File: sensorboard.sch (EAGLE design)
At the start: 34 parts, among them U1 LM1117MP-3.3, U2 LM324D

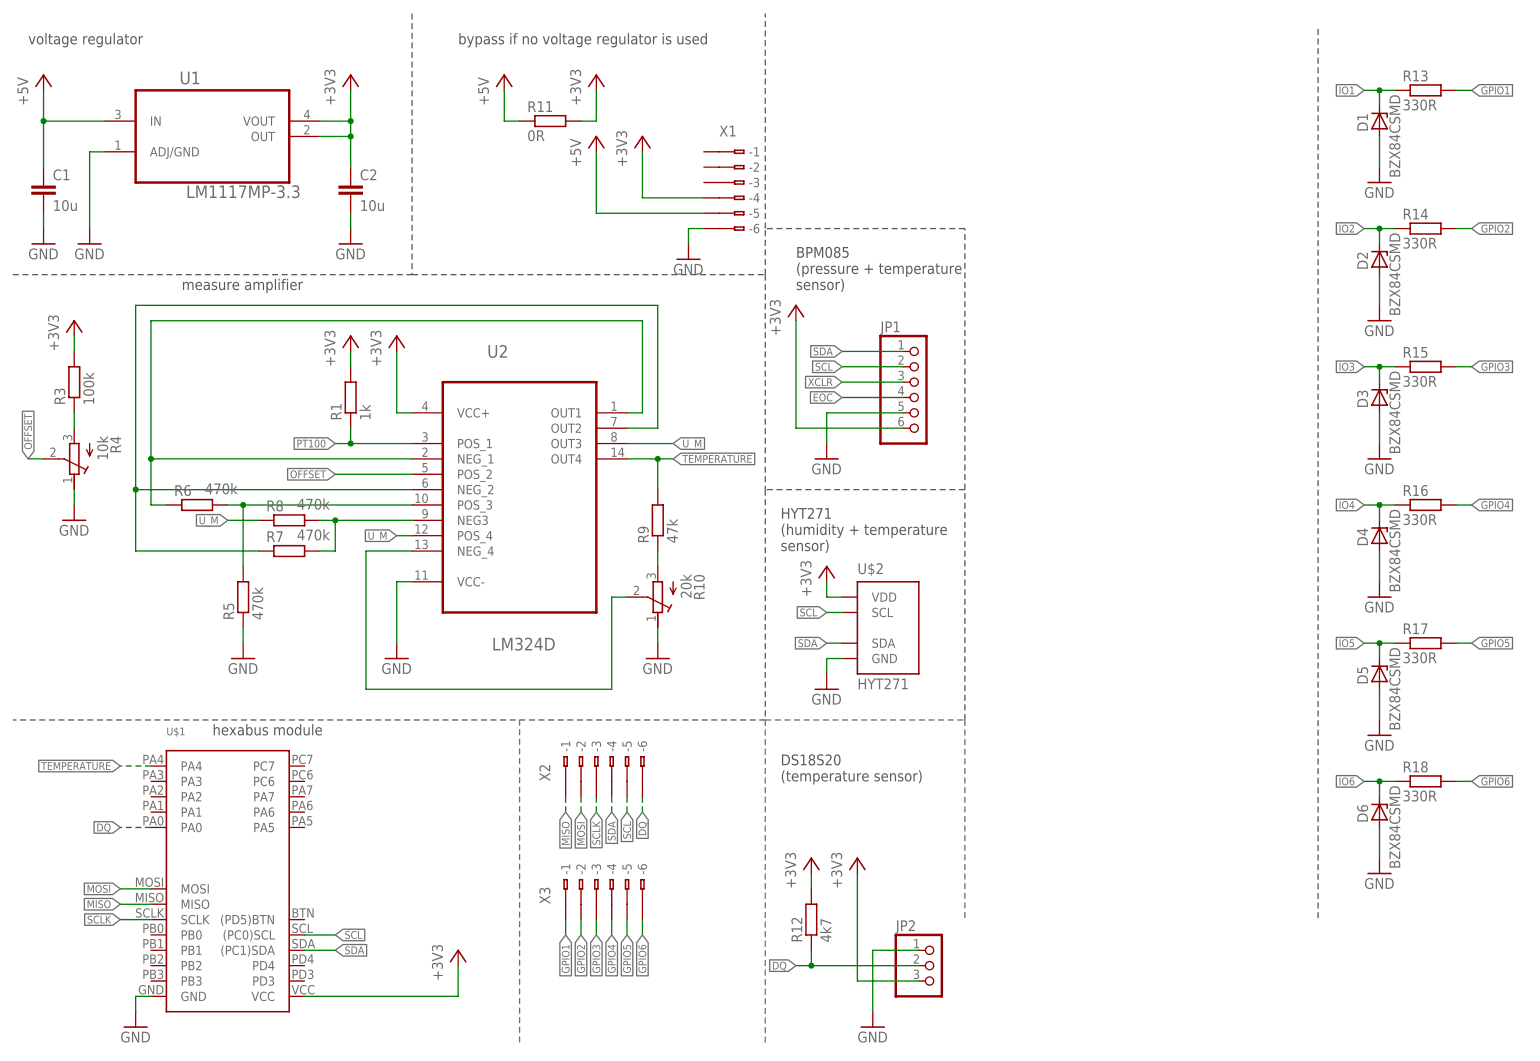
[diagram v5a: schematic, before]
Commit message: added button
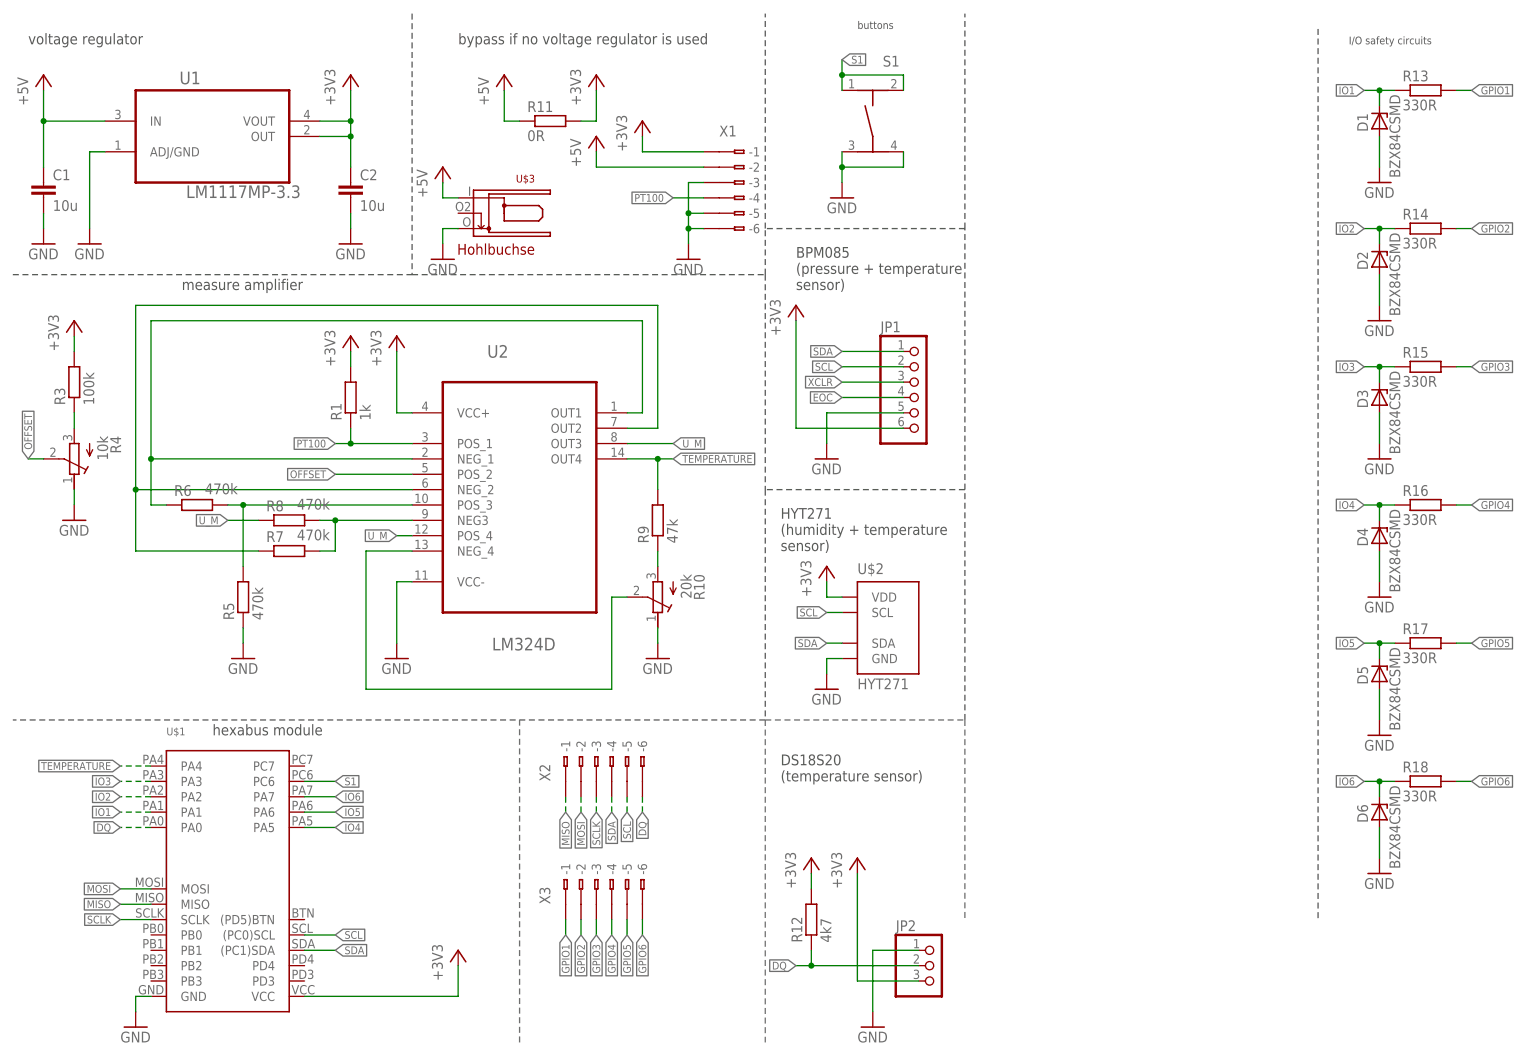
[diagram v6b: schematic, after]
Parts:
- added S1: (no value), Ergaenzung:TASTER-9314_SMD
- added U$3: HOHLBUCHSE, Ergaenzung:HOHLBUCHSE
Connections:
- new net S1: S1.1, S1.2, U$1.PC6
- net +3V3: now also X1.B-1; no longer X1.B-4
- net +5V: now also U$3.I, X1.B-2; no longer X1.B-5
- net GND: now also S1.3, S1.4, U$3.O, X1.B-3, X1.B-5
- net IO1: now also U$1.PA1
- net IO2: now also U$1.PA2
- net IO3: now also U$1.PA3
- net IO4: now also U$1.PA5
- net IO5: now also U$1.PA6
- net IO6: now also U$1.PA7
- net PT100: now also X1.B-4
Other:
- note added: "I/O safety circuits"
- note added: "buttons"
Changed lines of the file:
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@@
 <part name="R16" library="rcl" deviceset="R-EU_" device="R0805" value="330R"/>
 <part name="GND18" library="supply1" deviceset="GND" device=""/>
+<part name="S1" library="Ergaenzung" deviceset="TASTER-9314_SMD" device=""/>
+<part name="U$3" library="Ergaenzung" deviceset="HOHLBUCHSE" device=""/>
+<part name="P+4" library="supply1" deviceset="+5V" device=""/>
+<part name="GND19" library="supply1" deviceset="GND" device=""/>
+<part name="GND20" library="supply1" deviceset="GND" device=""/>
 </parts>
 <sheets>
@@
 <wire x1="162.56" y1="139.7" x2="129.54" y2="139.7" width="0.1524" layer="97" style="longdash"/>
 <wire x1="220.98" y1="172.72" x2="220.98" y2="25.4" width="0.1524" layer="97" style="longdash"/>
+<wire x1="162.56" y1="139.7" x2="162.56" y2="175.26" width="0.1524" layer="97" style="longdash"/>
+<text x="226.06" y="170.18" size="1.27" layer="97">I/O safety circuits</text>
+<text x="144.78" y="172.72" size="1.27" layer="97">buttons</text>
 </plain>
 <instances>
@@
 <instance part="X1" gate="G$1" x="127" y="147.32"/>
 <instance part="GND10" gate="1" x="116.84" y="134.62"/>
-<instance part="+3V10" gate="G$1" x="109.22" y="154.94"/>
+<instance part="+3V10" gate="G$1" x="109.22" y="157.48"/>
 <instance part="P+3" gate="1" x="101.6" y="154.94"/>
 <instance part="U$2" gate="A" x="149.86" y="73.66"/>
@@
 <instance part="R16" gate="G$1" x="238.76" y="93.98"/>
 <instance part="GND18" gate="1" x="231.14" y="78.74"/>
+<instance part="S1" gate="G$1" x="147.32" y="157.48"/>
+<instance part="U$3" gate="G$1" x="91.44" y="142.24" rot="R180"/>
+<instance part="P+4" gate="1" x="76.2" y="149.86"/>
+<instance part="GND19" gate="1" x="76.2" y="134.62"/>
+<instance part="GND20" gate="1" x="142.24" y="144.78"/>
 </instances>
 <busses>
@@
 <wire x1="119.38" y1="139.7" x2="116.84" y2="139.7" width="0.1524" layer="91"/>
 <wire x1="116.84" y1="139.7" x2="116.84" y2="137.16" width="0.1524" layer="91"/>
+<pinref part="X1" gate="G$1" pin="B-3"/>
+<wire x1="119.38" y1="147.32" x2="116.84" y2="147.32" width="0.1524" layer="91"/>
+<wire x1="116.84" y1="147.32" x2="116.84" y2="142.24" width="0.1524" layer="91"/>
+<junction x="116.84" y="139.7"/>
+<pinref part="X1" gate="G$1" pin="B-5"/>
+<wire x1="116.84" y1="142.24" x2="116.84" y2="139.7" width="0.1524" layer="91"/>
+<wire x1="119.38" y1="142.24" x2="116.84" y2="142.24" width="0.1524" layer="91"/>
+<junction x="116.84" y="142.24"/>
 </segment>
 <segment>
@@
 <pinref part="GND18" gate="1" pin="GND"/>
 <wire x1="231.14" y1="86.36" x2="231.14" y2="81.28" width="0.1524" layer="91"/>
+</segment>
+<segment>
+<pinref part="U$3" gate="G$1" pin="O"/>
+<pinref part="GND19" gate="1" pin="GND"/>
+<wire x1="78.74" y1="139.7" x2="76.2" y2="139.7" width="0.1524" layer="91"/>
+<wire x1="76.2" y1="139.7" x2="76.2" y2="137.16" width="0.1524" layer="91"/>
+</segment>
+<segment>
+<pinref part="S1" gate="G$1" pin="4"/>
+<wire x1="152.4" y1="152.4" x2="152.4" y2="149.86" width="0.1524" layer="91"/>
+<wire x1="152.4" y1="149.86" x2="142.24" y2="149.86" width="0.1524" layer="91"/>
+<pinref part="S1" gate="G$1" pin="3"/>
+<wire x1="142.24" y1="149.86" x2="142.24" y2="152.4" width="0.1524" layer="91"/>
+<pinref part="GND20" gate="1" pin="GND"/>
+<wire x1="142.24" y1="147.32" x2="142.24" y2="149.86" width="0.1524" layer="91"/>
+<junction x="142.24" y="149.86"/>
 </segment>
 </net>
@@
 </segment>
 <segment>
-<pinref part="X1" gate="G$1" pin="B-4"/>
-<pinref part="+3V10" gate="G$1" pin="+3V3"/>
-<wire x1="119.38" y1="144.78" x2="109.22" y2="144.78" width="0.1524" layer="91"/>
-<wire x1="109.22" y1="144.78" x2="109.22" y2="152.4" width="0.1524" layer="91"/>
-</segment>
-<segment>
 <pinref part="U$2" gate="A" pin="VDD"/>
 <pinref part="+3V11" gate="G$1" pin="+3V3"/>
 <wire x1="142.24" y1="78.74" x2="139.7" y2="78.74" width="0.1524" layer="91"/>
 <wire x1="139.7" y1="78.74" x2="139.7" y2="81.28" width="0.1524" layer="91"/>
+</segment>
+<segment>
+<pinref part="X1" gate="G$1" pin="B-1"/>
+<pinref part="+3V10" gate="G$1" pin="+3V3"/>
+<wire x1="119.38" y1="152.4" x2="109.22" y2="152.4" width="0.1524" layer="91"/>
+<wire x1="109.22" y1="152.4" x2="109.22" y2="154.94" width="0.1524" layer="91"/>
 </segment>
 </net>
@@
 </segment>
 <segment>
-<pinref part="X1" gate="G$1" pin="B-5"/>
+<pinref part="U$3" gate="G$1" pin="I"/>
+<pinref part="P+4" gate="1" pin="+5V"/>
+<wire x1="78.74" y1="144.78" x2="76.2" y2="144.78" width="0.1524" layer="91"/>
+<wire x1="76.2" y1="144.78" x2="76.2" y2="147.32" width="0.1524" layer="91"/>
+</segment>
+<segment>
+<pinref part="X1" gate="G$1" pin="B-2"/>
 <pinref part="P+3" gate="1" pin="+5V"/>
-<wire x1="119.38" y1="142.24" x2="101.6" y2="142.24" width="0.1524" layer="91"/>
-<wire x1="101.6" y1="142.24" x2="101.6" y2="152.4" width="0.1524" layer="91"/>
+<wire x1="119.38" y1="149.86" x2="101.6" y2="149.86" width="0.1524" layer="91"/>
+<wire x1="101.6" y1="149.86" x2="101.6" y2="152.4" width="0.1524" layer="91"/>
 </segment>
 </net>
@@
 <junction x="60.96" y="104.14"/>
 <label x="58.42" y="104.14" size="1.27" layer="95" rot="R180" xref="yes"/>
+</segment>
+<segment>
+<pinref part="X1" gate="G$1" pin="B-4"/>
+<wire x1="119.38" y1="144.78" x2="114.3" y2="144.78" width="0.1524" layer="91"/>
+<label x="114.3" y="144.78" size="1.27" layer="95" rot="R180" xref="yes"/>
 </segment>
 </net>
@@
 <label x="228.6" y="48.26" size="1.27" layer="95" rot="R180" xref="yes"/>
 </segment>
+<segment>
+<pinref part="U$1" gate="G$1" pin="PA7"/>
+<wire x1="53.34" y1="45.72" x2="58.42" y2="45.72" width="0.1524" layer="91"/>
+<label x="58.42" y="45.72" size="1.27" layer="95" xref="yes"/>
+</segment>
 </net>
 <net name="IO1" class="0">
@@
 <label x="228.6" y="162.56" size="1.27" layer="95" rot="R180" xref="yes"/>
 </segment>
+<segment>
+<pinref part="U$1" gate="G$1" pin="PA1"/>
+<wire x1="27.94" y1="43.18" x2="22.86" y2="43.18" width="0.1524" layer="91" style="longdash"/>
+<label x="22.86" y="43.18" size="1.27" layer="95" rot="R180" xref="yes"/>
+</segment>
 </net>
 <net name="IO2" class="0">
@@
 <label x="228.6" y="139.7" size="1.27" layer="95" rot="R180" xref="yes"/>
 </segment>
+<segment>
+<pinref part="U$1" gate="G$1" pin="PA2"/>
+<wire x1="27.94" y1="45.72" x2="22.86" y2="45.72" width="0.1524" layer="91" style="longdash"/>
+<label x="22.86" y="45.72" size="1.27" layer="95" rot="R180" xref="yes"/>
+</segment>
 </net>
 <net name="IO3" class="0">
@@
 <label x="228.6" y="116.84" size="1.27" layer="95" rot="R180" xref="yes"/>
 </segment>
+<segment>
+<pinref part="U$1" gate="G$1" pin="PA3"/>
+<wire x1="27.94" y1="48.26" x2="22.86" y2="48.26" width="0.1524" layer="91" style="longdash"/>
+<label x="22.86" y="48.26" size="1.27" layer="95" rot="R180" xref="yes"/>
+</segment>
 </net>
 <net name="IO4" class="0">
@@
 <label x="228.6" y="93.98" size="1.27" layer="95" rot="R180" xref="yes"/>
 </segment>
+<segment>
+<pinref part="U$1" gate="G$1" pin="PA5"/>
+<wire x1="53.34" y1="40.64" x2="58.42" y2="40.64" width="0.1524" layer="91"/>
+<label x="58.42" y="40.64" size="1.27" layer="95" xref="yes"/>
+</segment>
 </net>
 <net name="IO5" class="0">
@@
 <label x="228.6" y="71.12" size="1.27" layer="95" rot="R180" xref="yes"/>
 </segment>
-</net>
+<segment>
+<pinref part="U$1" gate="G$1" pin="PA6"/>
+<wire x1="53.34" y1="43.18" x2="58.42" y2="43.18" width="0.1524" layer="91"/>
+<label x="58.42" y="43.18" size="1.27" layer="95" xref="yes"/>
+</segment>
+</net>
+<net name="S1" class="0">
+<segment>
+<pinref part="S1" gate="G$1" pin="2"/>
+<wire x1="152.4" y1="162.56" x2="152.4" y2="165.1" width="0.1524" layer="91"/>
+<wire x1="152.4" y1="165.1" x2="142.24" y2="165.1" width="0.1524" layer="91"/>
+<pinref part="S1" gate="G$1" pin="1"/>
+<wire x1="142.24" y1="165.1" x2="142.24" y2="162.56" width="0.1524" layer="91"/>
+<wire x1="142.24" y1="165.1" x2="142.24" y2="167.64" width="0.1524" layer="91"/>
+<junction x="142.24" y="165.1"/>
+<label x="142.24" y="167.64" size="1.27" layer="95" xref="yes"/>
+</segment>
+<segment>
+<pinref part="U$1" gate="G$1" pin="PC6"/>
+<wire x1="53.34" y1="48.26" x2="58.42" y2="48.26" width="0.1524" layer="91"/>
+<label x="58.42" y="48.26" size="1.27" layer="95" xref="yes"/>
+</segment>
+</net>

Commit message: added led driver. Unused pins to a pinheader
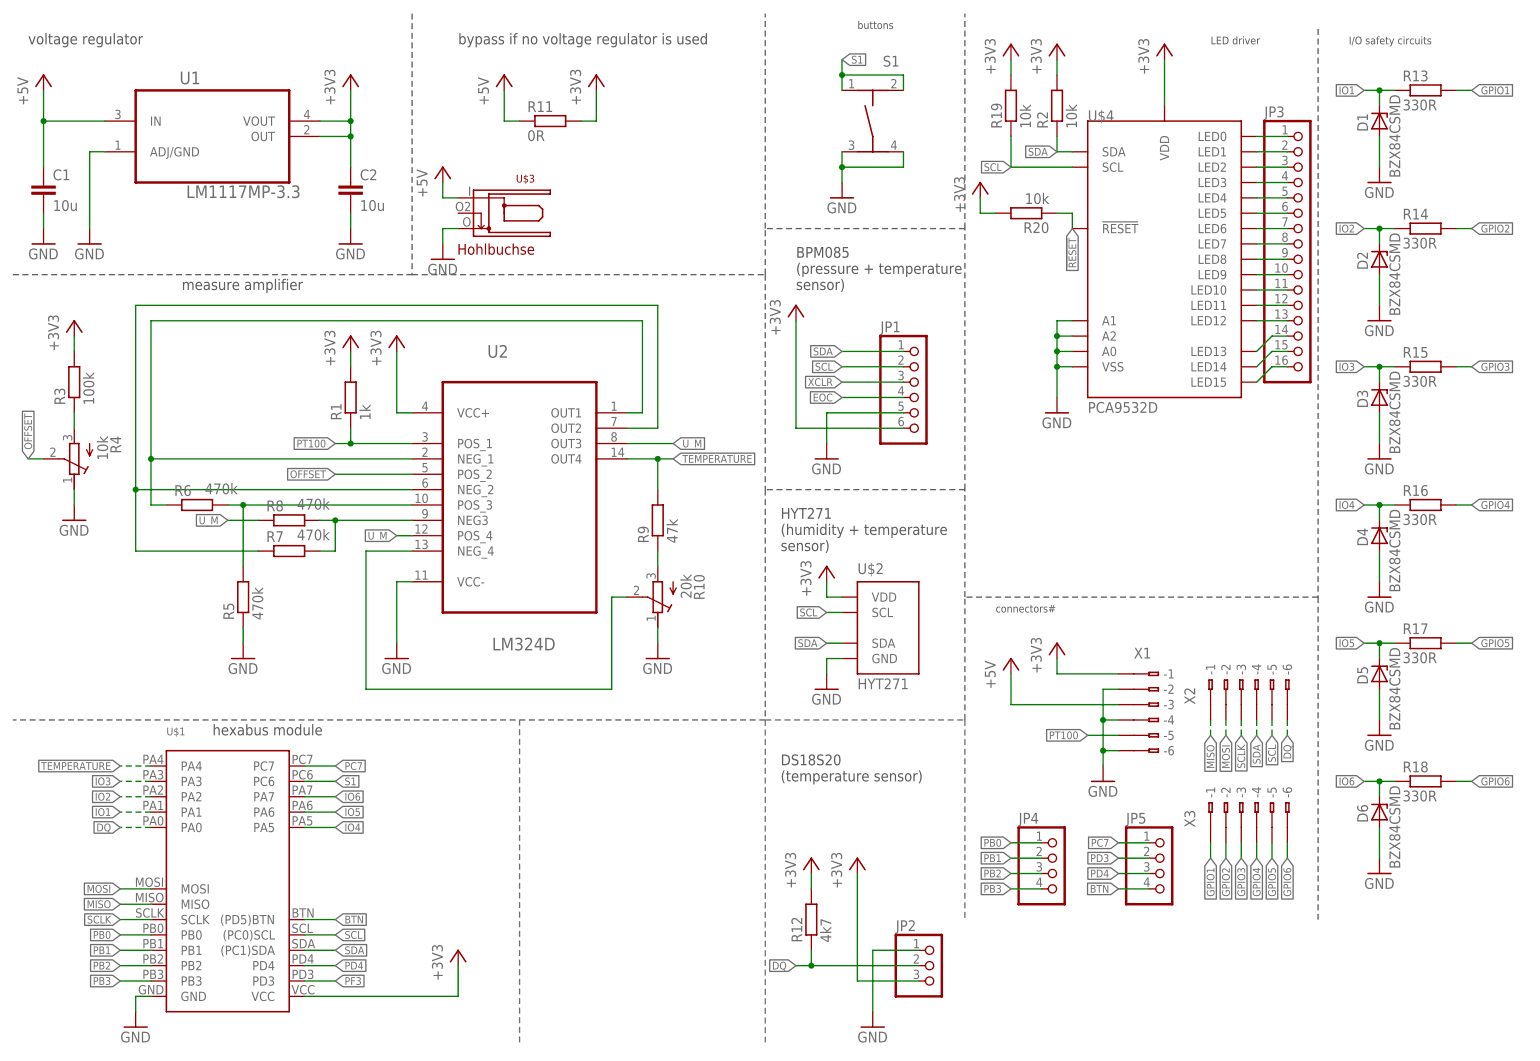
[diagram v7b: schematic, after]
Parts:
- added JP3: (no value), pinhead:PINHD-1X16
- added JP4, JP5: (no value), pinhead:PINHD-1X4
- added R19, R2, R20: 10k, rcl:R-EU_R0805
- added U$4: PCA9532D, philips:PCA9532D
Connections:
- new net !RESET: R20.1, U$4.!RESET
- new net BTN: JP5.4, U$1.(PD5)BTN
- new net N$10: JP3.3, U$4.LED2
- new net N$11: JP3.4, U$4.LED3
- new net N$12: JP3.5, U$4.LED4
- new net N$13: JP3.6, U$4.LED5
- new net N$14: JP3.7, U$4.LED6
- new net N$15: JP3.8, U$4.LED7
- new net N$16: JP3.9, U$4.LED8
- new net N$17: JP3.10, U$4.LED9
- new net N$18: JP3.11, U$4.LED10
- new net N$19: JP3.12, U$4.LED11
- new net N$20: JP3.13, U$4.LED12
- new net N$21: JP3.14, U$4.LED13
- new net N$22: JP3.15, U$4.LED14
- new net N$23: JP3.16, U$4.LED15
- new net N$8: JP3.1, U$4.LED0
- new net N$9: JP3.2, U$4.LED1
- new net PB0: JP4.1, U$1.PB0
- new net PB1: JP4.2, U$1.PB1
- new net PB2: JP4.3, U$1.PB2
- new net PB3: JP4.4, U$1.PB3
- new net PC7: JP5.1, U$1.PC7
- new net PD3: JP5.2
- new net PD4: JP5.3, U$1.PD4
- new net PF3: U$1.PD3
- net +3V3: now also R19.2, R2.2, R20.2, U$4.VDD
- net +5V: now also X1.B-3; no longer X1.B-2
- net GND: now also U$4.A0, U$4.A1, U$4.A2, U$4.VSS, X1.B-2, X1.B-4; no longer X1.B-3, X1.B-5
- net PT100: now also X1.B-5; no longer X1.B-4
- net SCL: now also R19.1, U$4.SCL
- net SDA: now also R2.1, U$4.SDA
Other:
- note added: "LED driver"
- note added: "connectors#"
- moved on the sheet: X1, X2, X3
